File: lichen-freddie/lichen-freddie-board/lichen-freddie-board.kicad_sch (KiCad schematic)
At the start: 37 parts, among them J1 3.5mm_Stereo, J2 Eurorack_Power

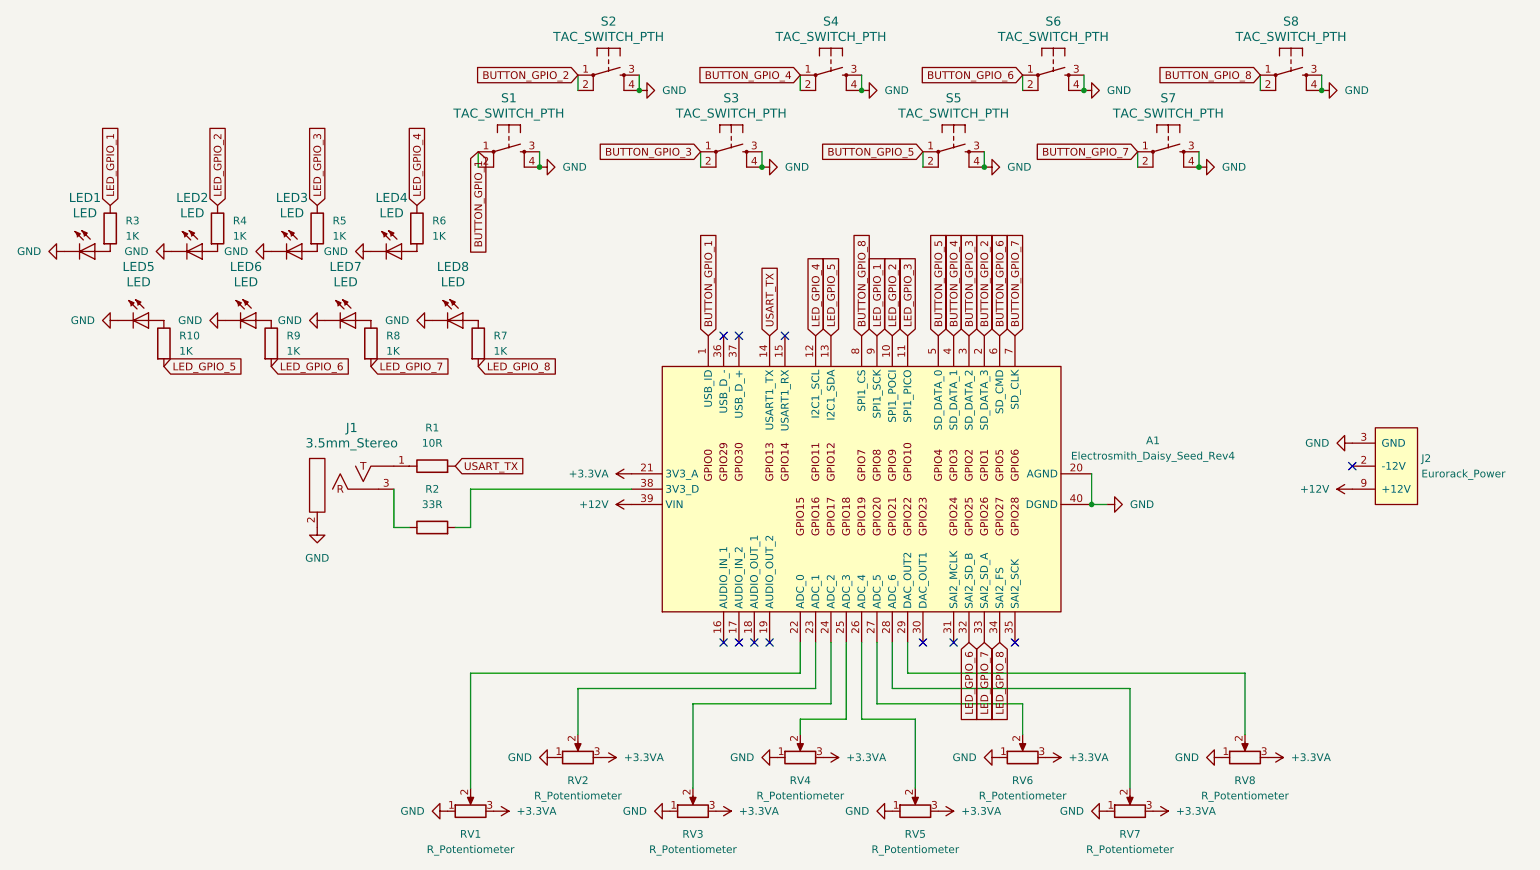
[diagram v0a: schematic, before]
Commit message: Updates Lichen component library and most module prototypes.
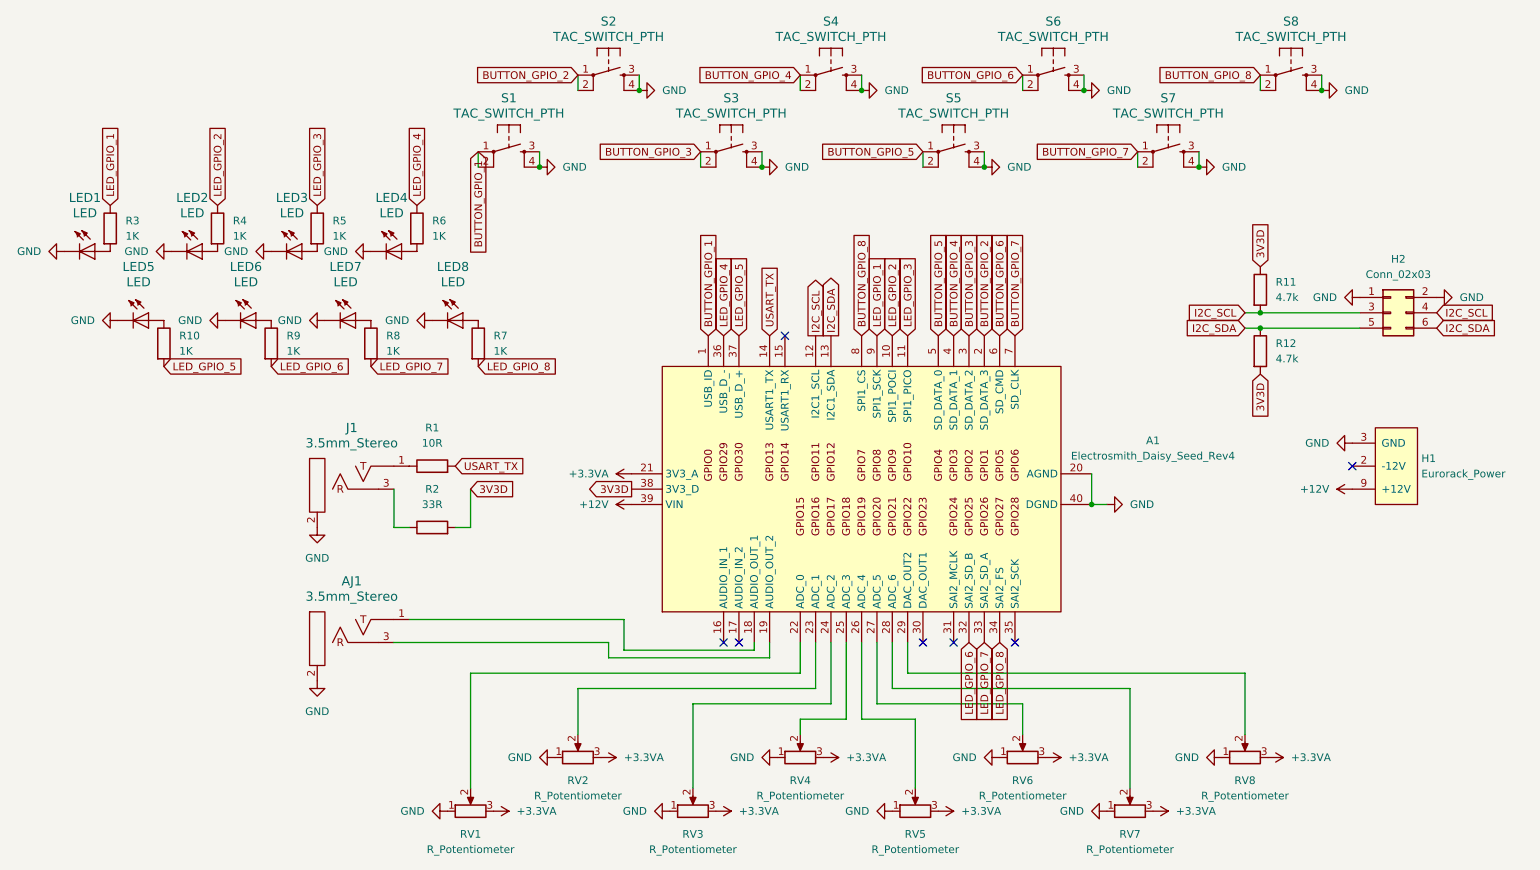
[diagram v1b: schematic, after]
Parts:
- added AJ1: 3.5mm_Stereo, PCM_4ms_Jack:EighthInch_Stereo_PJ366ST, symbol PCM_4ms_Jack:3.5mm_Stereo
- added H2: Conn_02x03, PCM_4ms_Connector:Pins_2x03_2.54mm_TH, symbol PCM_4ms_Connector:Conn_02x03
- added R11, R12: 4.7k_0603, PCM_4ms_Resistor:R_0603, symbol PCM_4ms_Resistor:4.7k_0603
- R10, R5, R6, R7, R8, R9: Part Number 0603WAF330JT5E -> 0603WAF1001T5E
- renumbered J2 to H1
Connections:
- net GND: now also AJ1.2 (SHEILD), H2.1 (+12V), H2.2 (+12V)
- net LED_GPIO_4: now also A1.36 (USB_D_-); no longer A1.12 (I2C1_SCL)
- net LED_GPIO_5: now also A1.37 (USB_D_+); no longer A1.13 (I2C1_SDA)
- net 3V3D: now reaches A1.38 (3V3_D), R2.2
- net 3V3D: now also R11.1, R12.2
- net at A1.18 (AUDIO_OUT_1): now also AJ1.1 (SIG)
- net at A1.19 (AUDIO_OUT_2): now also AJ1.3 (SW)
- new net I2C_SCL: A1.12 (I2C1_SCL), H2.3 (GND), H2.4 (GND), R11.2
- new net I2C_SDA: A1.13 (I2C1_SDA), H2.5 (GND), H2.6 (GND), R12.1
- no-connect marks 11 -> 7
